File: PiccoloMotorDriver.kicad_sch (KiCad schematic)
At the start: 7 parts

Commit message: Circular pcb edge cut
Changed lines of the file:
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@@
 	(generator_version "9.0")
 	(paper "A5")
+	(text_box "TODO\n"
+		(exclude_from_sim no)
+		(at 133.35 20.32 0)
+		(size 62.23 55.88)
+		(margins 0.9525 0.9525 0.9525 0.9525)
+		(stroke
+			(width 0)
+			(type solid)
+			(color 255 245 0 1)
+		)
+		(fill
+			(type none)
+		)
+		(effects
+			(font
+				(size 1.27 1.27)
+				(thickness 0.1588)
+			)
+			(justify left top)
+		)
+	)
 	(junction
 		(at 34.29 123.19)
@@
 	)
 	(sheet
-		(at 124.46 19.05)
+		(at 105.41 20.32)
 		(size 24.13 24.13)
 		(exclude_from_sim no)
@@
 		)
 		(property "Sheetname" "IO"
-			(at 124.46 18.3384 0)
+			(at 105.41 19.6084 0)
 			(effects
 				(font
@@
 		)
 		(property "Sheetfile" "IO.kicad_sch"
-			(at 124.46 43.7646 0)
+			(at 105.41 45.0346 0)
 			(effects
 				(font
@@
 	)
 	(sheet
-		(at 83.82 19.05)
+		(at 64.77 20.32)
 		(size 26.67 55.88)
 		(exclude_from_sim no)
@@
 		)
 		(property "Sheetname" "Mcu"
-			(at 83.82 18.3384 0)
+			(at 64.77 19.6084 0)
 			(effects
 				(font
@@
 		)
 		(property "Sheetfile" "Mcu.kicad_sch"
-			(at 83.82 75.5146 0)
+			(at 64.77 76.7846 0)
 			(effects
 				(font
@@
 	)
 	(sheet
-		(at 124.46 50.8)
+		(at 105.41 52.07)
 		(size 24.13 24.13)
 		(exclude_from_sim no)
@@
 		)
 		(property "Sheetname" "Inverter"
-			(at 124.46 50.0884 0)
+			(at 105.41 51.3584 0)
 			(effects
 				(font
@@
 		)
 		(property "Sheetfile" "DRV.kicad_sch"
-			(at 124.46 75.5146 0)
+			(at 105.41 76.7846 0)
 			(effects
 				(font
@@
 	)
 	(sheet
-		(at 46.99 50.8)
+		(at 27.94 52.07)
 		(size 24.13 24.13)
 		(exclude_from_sim no)
@@
 		)
 		(property "Sheetname" "Encoder"
-			(at 46.99 50.0884 0)
+			(at 27.94 51.3584 0)
 			(effects
 				(font
@@
 		)
 		(property "Sheetfile" "Encoder.kicad_sch"
-			(at 46.99 75.5146 0)
+			(at 27.94 76.7846 0)
 			(effects
 				(font
@@
 	)
 	(sheet
-		(at 46.99 19.05)
+		(at 27.94 20.32)
 		(size 24.13 24.13)
 		(exclude_from_sim no)
@@
 		)
 		(property "Sheetname" "PowerManagement"
-			(at 46.99 18.3384 0)
+			(at 27.94 19.6084 0)
 			(effects
 				(font
@@
 		)
 		(property "Sheetfile" "PowerManagement.kicad_sch"
-			(at 46.99 43.7646 0)
-			(effects
-				(font
+			(at 27.94 45.0346 0)
+			(effects
+				(font

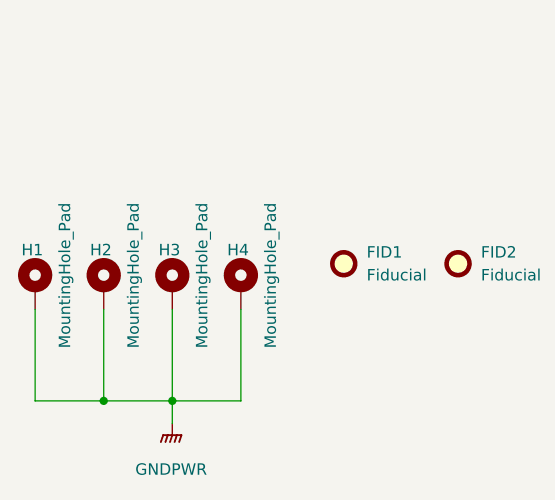
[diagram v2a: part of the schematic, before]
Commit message: More layout, add can,rs485 leds
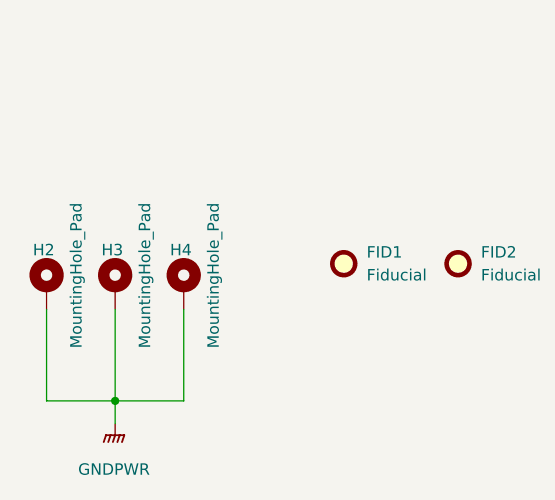
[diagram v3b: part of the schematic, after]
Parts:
- removed H1: MountingHole_Pad, MountingHole:MountingHole_3.2mm_M3_Pad_Via, symbol Mechanical:MountingHole_Pad
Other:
- moved on the sheet: H2, H3, H4
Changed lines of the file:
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@@
 	)
 	(junction
-		(at 34.29 123.19)
+		(at 27.94 123.19)
 		(diameter 0)
 		(color 0 0 0 0)
 	)
-	(junction
-		(at 26.67 123.19)
-		(diameter 0)
-		(color 0 0 0 0)
-	)
 	(wire
 		(pts
-			(xy 34.29 123.19) (xy 34.29 125.73)
+			(xy 27.94 123.19) (xy 27.94 125.73)
 		)
 		(stroke
@@
 	(wire
 		(pts
-			(xy 34.29 113.03) (xy 34.29 123.19)
+			(xy 27.94 113.03) (xy 27.94 123.19)
 		)
 		(stroke
@@
 	(wire
 		(pts
-			(xy 19.05 113.03) (xy 19.05 123.19)
+			(xy 27.94 123.19) (xy 35.56 123.19)
 		)
 		(stroke
@@
 	(wire
 		(pts
-			(xy 34.29 123.19) (xy 41.91 123.19)
+			(xy 20.32 113.03) (xy 20.32 123.19)
 		)
 		(stroke
@@
 	(wire
 		(pts
-			(xy 26.67 113.03) (xy 26.67 123.19)
+			(xy 20.32 123.19) (xy 27.94 123.19)
 		)
 		(stroke
@@
 	(wire
 		(pts
-			(xy 26.67 123.19) (xy 34.29 123.19)
+			(xy 35.56 123.19) (xy 35.56 113.03)
 		)
 		(stroke
@@
 		)
 	)
-	(wire
-		(pts
-			(xy 19.05 123.19) (xy 26.67 123.19)
-		)
-		(stroke
-			(width 0)
-			(type default)
-		)
-	)
-	(wire
-		(pts
-			(xy 41.91 123.19) (xy 41.91 113.03)
-		)
-		(stroke
-			(width 0)
-			(type default)
-		)
-	)
 	(symbol
 		(lib_id "power:GNDPWR")
-		(at 34.29 125.73 0)
+		(at 27.94 125.73 0)
 		(unit 1)
 		(body_style 1)
@@
 		(fields_autoplaced yes)
 		(property "Reference" "#PWR061"
-			(at 34.29 130.81 0)
+			(at 27.94 130.81 0)
 			(hide yes)
 			(show_name no)
@@
 		)
 		(property "Value" "GNDPWR"
-			(at 34.163 130.81 0)
+			(at 27.813 130.81 0)
 			(show_name no)
 			(do_not_autoplace no)
@@
 		)
 		(property "Footprint" ""
-			(at 34.29 127 0)
-			(hide yes)
-			(show_name no)
-			(do_not_autoplace no)
-			(effects
-				(font
-					(size 1.27 1.27)
-				)
-			)
-		)
-		(property "Datasheet" ""
-			(at 34.29 127 0)
+			(at 27.94 127 0)
+			(hide yes)
+			(show_name no)
+			(do_not_autoplace no)
+			(effects
+				(font
+					(size 1.27 1.27)
+				)
+			)
+		)
+		(property "Datasheet" ""
+			(at 27.94 127 0)
 			(hide yes)
 			(show_name no)
@@
 		)
 		(property "Description" ""
-			(at 34.29 125.73 0)
+			(at 27.94 125.73 0)
 			(show_name no)
 			(do_not_autoplace no)
@@
 	(symbol
 		(lib_id "Mechanical:MountingHole_Pad")
-		(at 26.67 110.49 0)
+		(at 20.32 110.49 0)
 		(unit 1)
 		(body_style 1)
@@
 		(dnp no)
 		(property "Reference" "H2"
-			(at 25.146 106.426 0)
+			(at 18.796 106.426 0)
 			(show_name no)
 			(do_not_autoplace no)
@@
 		)
 		(property "Value" "MountingHole_Pad"
-			(at 29.972 117.348 90)
+			(at 23.622 117.348 90)
 			(show_name no)
 			(do_not_autoplace no)
@@
 		)
 		(property "Footprint" "MountingHole:MountingHole_3.2mm_M3_Pad_Via"
-			(at 26.67 110.49 0)
-			(hide yes)
-			(show_name no)
-			(do_not_autoplace no)
-			(effects
-				(font
-					(size 1.27 1.27)
-				)
-			)
-		)
-		(property "Datasheet" ""
-			(at 26.67 110.49 0)
+			(at 20.32 110.49 0)
+			(hide yes)
+			(show_name no)
+			(do_not_autoplace no)
+			(effects
+				(font
+					(size 1.27 1.27)
+				)
+			)
+		)
+		(property "Datasheet" ""
+			(at 20.32 110.49 0)
 			(hide yes)
 			(show_name no)
@@
 		)
 		(property "Description" "Mounting Hole with connection"
-			(at 26.67 110.49 0)
+			(at 20.32 110.49 0)
 			(hide yes)
 			(show_name no)
@@
 	(symbol
 		(lib_id "Mechanical:MountingHole_Pad")
-		(at 34.29 110.49 0)
+		(at 27.94 110.49 0)
 		(unit 1)
 		(body_style 1)
@@
 		(dnp no)
 		(property "Reference" "H3"
-			(at 32.766 106.426 0)
+			(at 26.416 106.426 0)
 			(show_name no)
 			(do_not_autoplace no)
@@
 		)
 		(property "Value" "MountingHole_Pad"
-			(at 37.592 117.348 90)
+			(at 31.242 117.348 90)
 			(show_name no)
 			(do_not_autoplace no)
@@
 		)
 		(property "Footprint" "MountingHole:MountingHole_3.2mm_M3_Pad_Via"
-			(at 34.29 110.49 0)
-			(hide yes)
-			(show_name no)
-			(do_not_autoplace no)
-			(effects
-				(font
-					(size 1.27 1.27)
-				)
-			)
-		)
-		(property "Datasheet" ""
-			(at 34.29 110.49 0)
+			(at 27.94 110.49 0)
+			(hide yes)
+			(show_name no)
+			(do_not_autoplace no)
+			(effects
+				(font
+					(size 1.27 1.27)
+				)
+			)
+		)
+		(property "Datasheet" ""
+			(at 27.94 110.49 0)
 			(hide yes)
 			(show_name no)
@@
 		)
 		(property "Description" "Mounting Hole with connection"
-			(at 34.29 110.49 0)
+			(at 27.94 110.49 0)
 			(hide yes)
 			(show_name no)
@@
 	)
 	(symbol
-		(lib_id "Mechanical:MountingHole_Pad")
-		(at 19.05 110.49 0)
-		(unit 1)
-		(body_style 1)
-		(exclude_from_sim no)
-		(in_bom no)
-		(on_board yes)
-		(in_pos_files yes)
-		(dnp no)
-		(property "Reference" "H1"
-			(at 17.526 106.426 0)
-			(show_name no)
-			(do_not_autoplace no)
-			(effects
-				(font
-					(size 1.27 1.27)
-				)
-				(justify left)
-			)
-		)
-		(property "Value" "MountingHole_Pad"
-			(at 22.352 117.348 90)
-			(show_name no)
-			(do_not_autoplace no)
-			(effects
-				(font
-					(size 1.27 1.27)
-				)
-				(justify left)
-			)
-		)
-		(property "Footprint" "MountingHole:MountingHole_3.2mm_M3_Pad_Via"
-			(at 19.05 110.49 0)
-			(hide yes)
-			(show_name no)
-			(do_not_autoplace no)
-			(effects
-				(font
-					(size 1.27 1.27)
-				)
-			)
-		)
-		(property "Datasheet" ""
-			(at 19.05 110.49 0)
-			(hide yes)
-			(show_name no)
-			(do_not_autoplace no)
-			(effects
-				(font
-					(size 1.27 1.27)
-				)
-			)
-		)
-		(property "Description" "Mounting Hole with connection"
-			(at 19.05 110.49 0)
-			(hide yes)
-			(show_name no)
-			(do_not_autoplace no)
-			(effects
-				(font
-					(size 1.27 1.27)
-				)
-			)
-		)
-		(pin "1"
-		)
-		(instances
-			(project "PiccoloMotorDriver"
-				(path "/cc8a13e7-b1a6-4cbd-adcd-4feb8b2e2369"
-					(reference "H1")
-					(unit 1)
-				)
-			)
-		)
-	)
-	(symbol
 		(lib_id "Mechanical:Fiducial")
 		(at 53.34 107.95 0)
@@
 	(symbol
 		(lib_id "Mechanical:MountingHole_Pad")
-		(at 41.91 110.49 0)
+		(at 35.56 110.49 0)
 		(unit 1)
 		(body_style 1)
@@
 		(dnp no)
 		(property "Reference" "H4"
-			(at 40.386 106.426 0)
+			(at 34.036 106.426 0)
 			(show_name no)
 			(do_not_autoplace no)
@@
 		)
 		(property "Value" "MountingHole_Pad"
-			(at 45.212 117.348 90)
+			(at 38.862 117.348 90)
 			(show_name no)
 			(do_not_autoplace no)
@@
 		)
 		(property "Footprint" "MountingHole:MountingHole_3.2mm_M3_Pad_Via"
-			(at 41.91 110.49 0)
-			(hide yes)
-			(show_name no)
-			(do_not_autoplace no)
-			(effects
-				(font
-					(size 1.27 1.27)
-				)
-			)
-		)
-		(property "Datasheet" ""
-			(at 41.91 110.49 0)
+			(at 35.56 110.49 0)
+			(hide yes)
+			(show_name no)
+			(do_not_autoplace no)
+			(effects
+				(font
+					(size 1.27 1.27)
+				)
+			)
+		)
+		(property "Datasheet" ""
+			(at 35.56 110.49 0)
 			(hide yes)
 			(show_name no)
@@
 		)
 		(property "Description" "Mounting Hole with connection"
-			(at 41.91 110.49 0)
-			(hide yes)
-			(show_name no)
+			(at 35.56 110.49 0)
+			(hide yes)
+			(show_name no)
